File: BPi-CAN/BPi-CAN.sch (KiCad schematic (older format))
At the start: 82 parts, among them J1 RJ45, J2 RJ45, J3 RJ45, J4 RJ45, P1 BPi, P10 SPI, P11 SNIFFER, P12 CAN-Bus, P13 USB, P14 CAN-Bus, P15 POWER, P16 CAN, P17 CAN, P18 CAN, P19 TERM, P2 S88, P20 S88 CONN, P21 RS232 Con, P22 S88, P3 CONN_02X04, P4 CONN_01X02, P5 TERM, P6 S88, P7 I2C-Bus, P8 RS485, P9 RS232, U1 MCP2562, U10 MCP2562, U11 6N137, U12 ISO1050, U13 FT230XS, U2 LM7805, U3 6N137, U4 6N137, U5 6N137, U6 6N137, U7 ADuM1251BR, U8 MAX3072E, U9 MAX3232

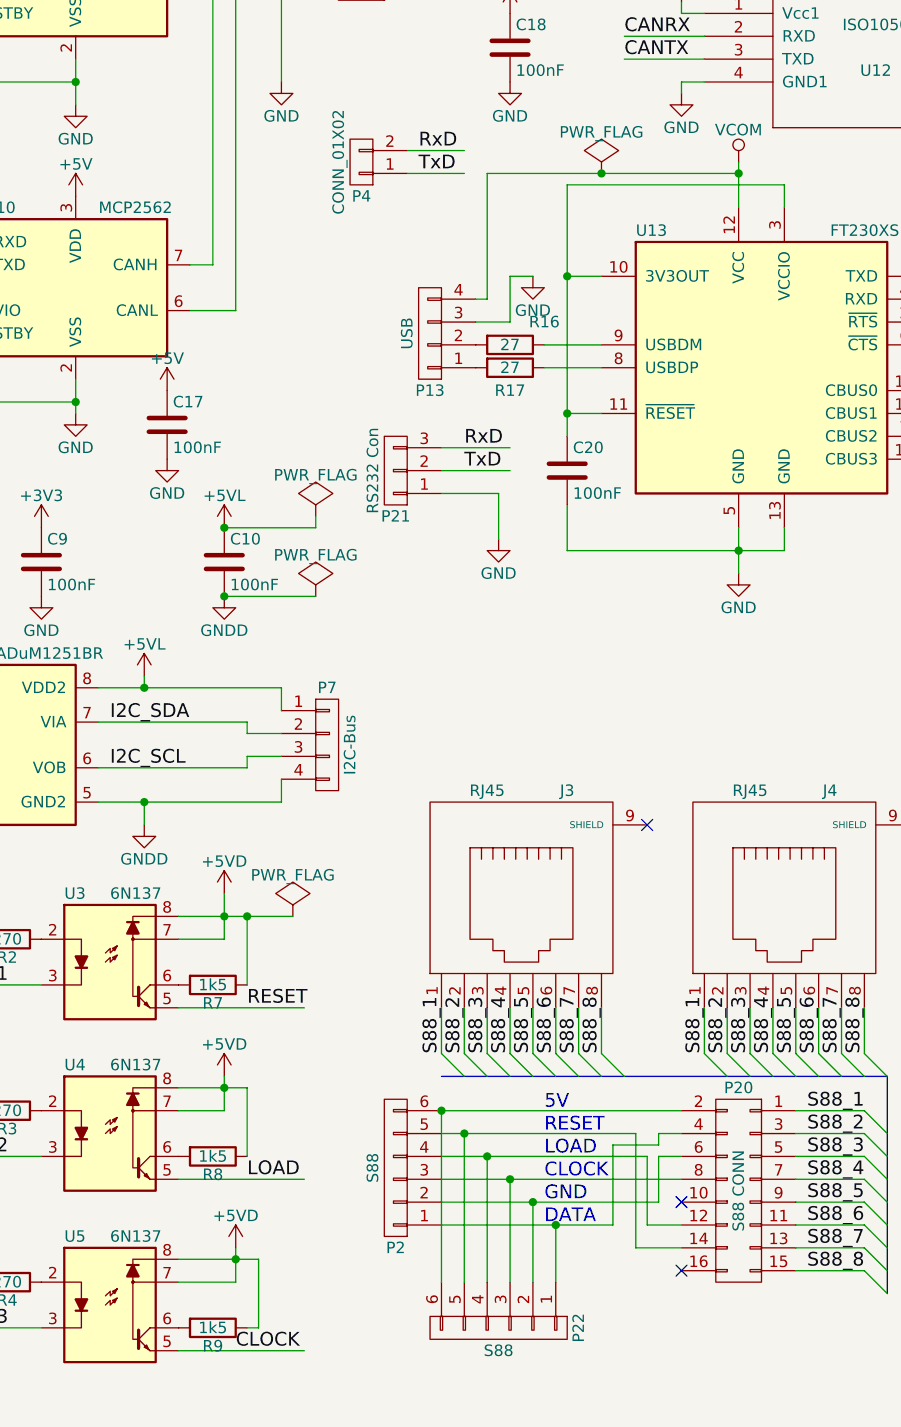
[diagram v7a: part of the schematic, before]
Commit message: add Schematic print
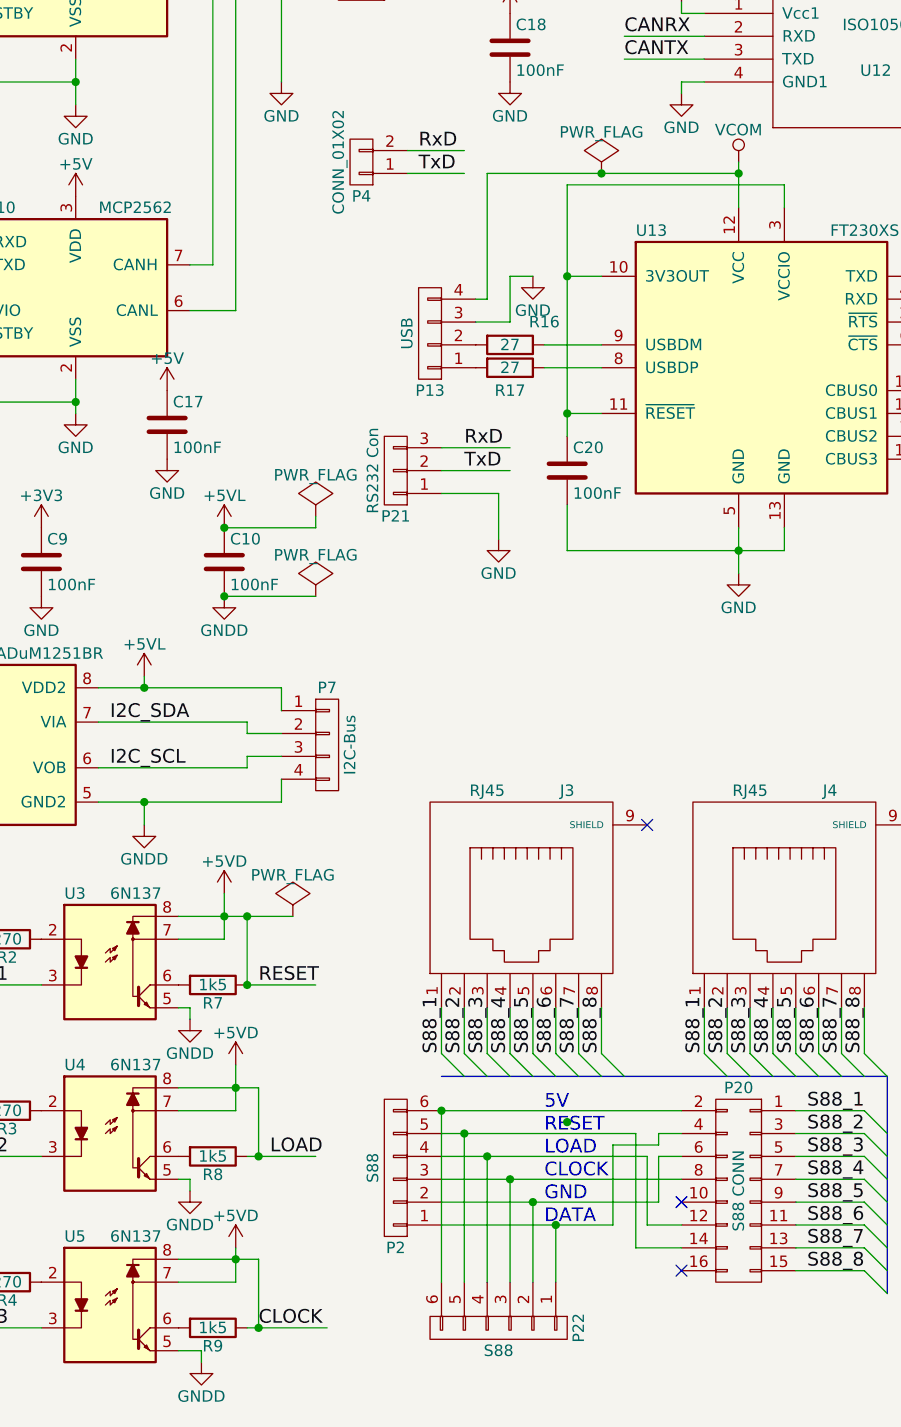
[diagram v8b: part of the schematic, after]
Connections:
- wire segments 347 -> 352
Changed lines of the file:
@@
 L +5VD #PWR018
 U 1 1 567EC957
-P 3850 6450
-F 0 "#PWR018" H 3850 6300 50  0001 C CNN
-F 1 "+5VD" H 3850 6590 50  0000 C CNN
-F 2 "" H 3850 6450 50  0000 C CNN
-F 3 "" H 3850 6450 50  0000 C CNN
-	1    3850 6450
+P 3900 6400
+F 0 "#PWR018" H 3900 6250 50  0001 C CNN
+F 1 "+5VD" H 3900 6540 50  0000 C CNN
+F 2 "" H 3900 6400 50  0000 C CNN
+F 3 "" H 3900 6400 50  0000 C CNN
+	1    3900 6400
 	1    0    0    -1
 $EndComp
@@
 Text Label 1300 6250 0    60   ~ 0
 DATA
-Text Label 3950 6150 0    60   ~ 0
+Text Label 4000 6050 0    60   ~ 0
 RESET
-Text Label 3950 6900 0    60   ~ 0
-LOAD
-Text Label 3900 7650 0    60   ~ 0
+Text Label 4000 7550 0    60   ~ 0
 CLOCK
 $Comp
@@
 Connection ~ 3900 7250
 Wire Wire Line
-	3850 6600 3650 6600
-Wire Wire Line
-	3850 6450 3850 6600
-Wire Wire Line
-	3650 6500 3950 6500
-Connection ~ 3850 6500
-Wire Wire Line
 	3050 6050 2650 6050
 Wire Wire Line
@@
 	3950 5750 3950 6050
 Wire Wire Line
-	3950 6500 3950 6800
-Wire Wire Line
-	3950 7550 4000 7550
-Wire Wire Line
-	4000 7550 4000 7250
-Wire Wire Line
-	3650 6150 4200 6150
-Wire Wire Line
-	3650 6900 4200 6900
-Wire Wire Line
-	3650 7650 4200 7650
+	3950 7550 4300 7550
+Wire Wire Line
+	4000 7250 4000 7550
 Wire Wire Line
 	1050 6150 1650 6150
@@
 	4600 1700 4850 1700
 Wire Wire Line
-	6100 2650 6100 2450
+	6100 2450 6100 2650
 Wire Bus Line
 	4800 6450 6750 6450
@@
 	600  6950 600  7300
 Wire Wire Line
-	6100 2500 5000 2500
+	5000 2500 6100 2500
 Connection ~ 6100 2500
 $Comp
@@
 $EndComp
 Connection ~ 3950 5750
+Wire Wire Line
+	3950 6050 4250 6050
+Connection ~ 4000 7550
+$Comp
+L GNDD #PWR081
+U 1 1 56937BF6
+P 3750 7700
+F 0 "#PWR081" H 3750 7450 50  0001 C CNN
+F 1 "GNDD" H 3750 7550 50  0000 C CNN
+F 2 "" H 3750 7700 50  0000 C CNN
+F 3 "" H 3750 7700 50  0000 C CNN
+	1    3750 7700
+	1    0    0    -1
+$EndComp
+$Comp
+L GNDD #PWR082
+U 1 1 56937CF7
+P 3700 6950
+F 0 "#PWR082" H 3700 6700 50  0001 C CNN
+F 1 "GNDD" H 3700 6800 50  0000 C CNN
+F 2 "" H 3700 6950 50  0000 C CNN
+F 3 "" H 3700 6950 50  0000 C CNN
+	1    3700 6950
+	1    0    0    -1
+$EndComp
+$Comp
+L GNDD #PWR083
+U 1 1 56937DF8
+P 3700 6200
+F 0 "#PWR083" H 3700 5950 50  0001 C CNN
+F 1 "GNDD" H 3700 6050 50  0000 C CNN
+F 2 "" H 3700 6200 50  0000 C CNN
+F 3 "" H 3700 6200 50  0000 C CNN
+	1    3700 6200
+	1    0    0    -1
+$EndComp
+Wire Wire Line
+	3650 6150 3700 6150
+Wire Wire Line
+	3700 6150 3700 6200
+Wire Wire Line
+	3650 6900 3700 6900
+Wire Wire Line
+	3700 6900 3700 6950
+Wire Wire Line
+	3650 7650 3750 7650
+Wire Wire Line
+	3750 7650 3750 7700
+Connection ~ 5350 6650
+Connection ~ 3950 6050
+Text Label 4050 6800 0    60   ~ 0
+LOAD
+Wire Wire Line
+	3950 6800 4250 6800
+Wire Wire Line
+	4000 6500 4000 6800
+Connection ~ 4000 6800
+Wire Wire Line
+	3650 6500 4000 6500
+Wire Wire Line
+	3900 6600 3650 6600
+Wire Wire Line
+	3900 6400 3900 6600
+Connection ~ 3900 6500
 $EndSCHEMATC
